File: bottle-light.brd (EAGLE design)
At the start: 160 x 100 mm, 49 parts, among them IC1 STM32F334K8T, IC2 LF33, T1 BC337, T2 BC337, T3 BC337

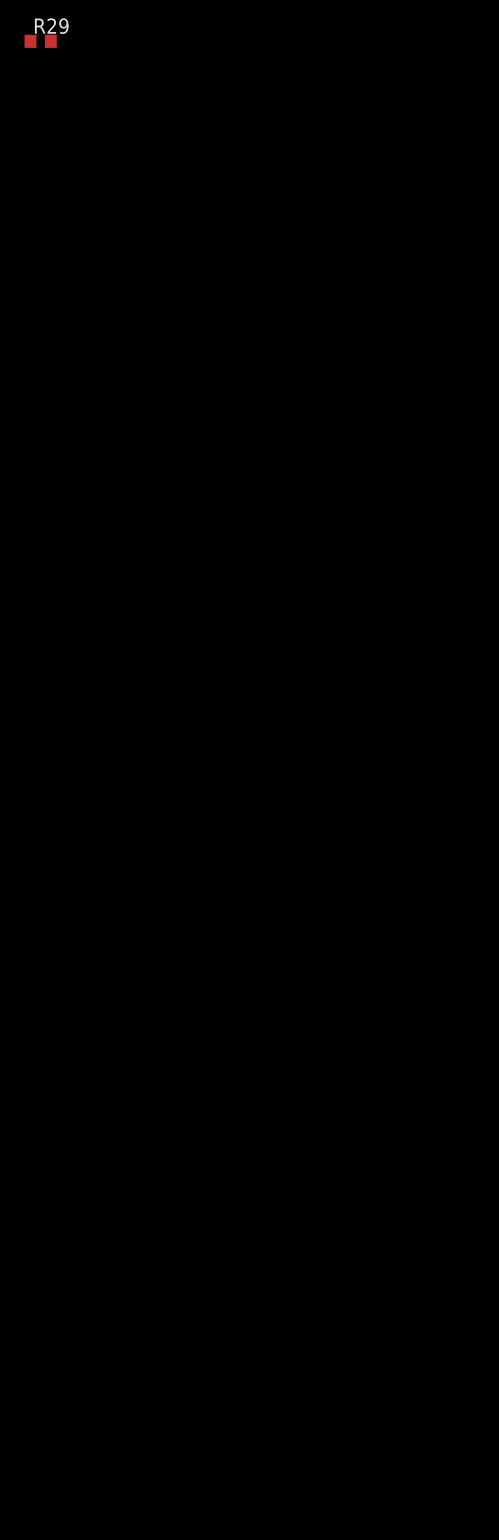
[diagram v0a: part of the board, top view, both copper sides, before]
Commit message: v0.1.1 worked on circuit diagram - new push buttons - new on/off button
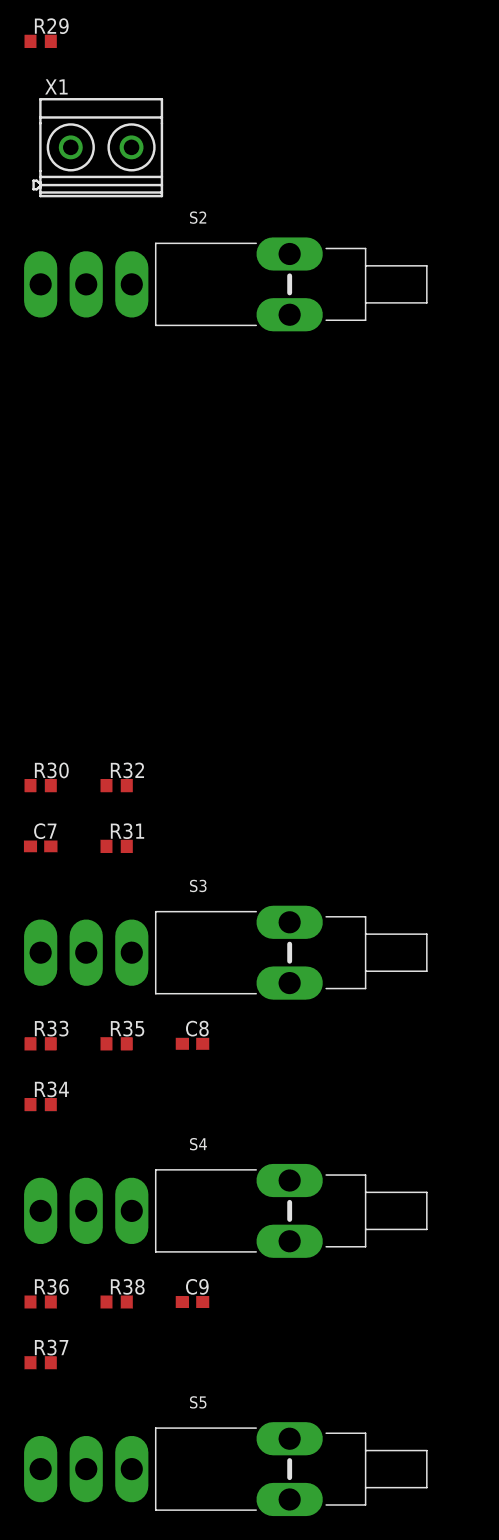
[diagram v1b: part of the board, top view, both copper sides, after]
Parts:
- added C7, C8, C9: 100n, resistor:C0603
- added R30, R33, R36: 100R, rcl:R0603
- added R31, R34, R37: 100k, rcl:R0603
- added R32, R35, R38: 330R, rcl:R0603
- added S2, S3, S4, S5: SPDT_PCB, h8-switch:SPDT_PCB
- added X1: 1725656, con-phoenix-508:MKDSN1,5/2-5,08
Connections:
- new net N$30: R30.1, R31.2, R32.2, S2.1
- new net N$31: C7.2, R30.2
- new net N$32: R33.1, R34.2, R35.2, S3.1
- new net N$33: C8.2, R33.2
- new net N$35: R36.1, R37.2, R38.2, S4.1
- new net N$36: C9.2, R36.2
- new net N$37: S5.1, X1.1
- new net USER-BUTTON1: R32.1
- new net USER-BUTTON2: R35.1
- new net USER-BUTTON3: R38.1
- net +3V3: now also C7.1, C8.1, C9.1, S2.2, S3.2, S4.2
- net +5V: now also S5.2
- net GND: now also R31.1, R34.1, R37.1, X1.2

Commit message: v0.1.2 Put in new devices and began routing pcb - new potis - made groundplane size for case - placed leds, potis and switch
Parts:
- LED1, LED2, LED3, LED4, LED5, LED6: value OSRAM_RGB-LED_LRTB-GFTM -> LRTB-GFTM
- R25, R26: value (none) -> RK09K; device pot:CIP20C-6MM -> h8-rlc:RK09K
- moved S2 158.4 mm to (7.00, 74.5), turned to 90 degrees
- moved R26 143.7 mm to (43.0, 83.5)
- moved LED3 108.9 mm to (58.0, 62.0)
- moved IC2 107.8 mm to (75.6, 59.3), turned to 180 degrees
- moved R25 105.2 mm to (25.0, 83.5)
- moved LED5 91.1 mm to (44.0, 46.0)
- moved LED4 90.2 mm to (66.0, 38.0)
- moved LED6 73.0 mm to (44.0, 22.0)
- moved LED1 68.9 mm to (22.0, 38.0)
- moved LED2 61.4 mm to (30.0, 62.0)
- moved IC1 0.38 mm to (-39.0, 5.00)
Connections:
- net +3V3: now also R25.3, R26.3; no longer R25.E, R26.E
- net GND: now also R25.1, R26.1; no longer R25.A, R26.A
- net POTI_COLOR: now also R25.2; no longer R25.S
- net POTI_LUMINOSITY: now also R26.2; no longer R26.S
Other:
- board size 160 x 100 mm -> 89 x 88 mm
- board text added: "Bottle Light | by HansAchterbahn v 0.1.2 | 09/07/2017"

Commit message: v0.1.3 schematic finished and board is routed - added new buttons - added swd debugger port - added battery pack - changed stm32 pinning - changed dc power supply port - removed reset button - added base resistors to transistors - routed board
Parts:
- removed S1: (no value), h8-switch:TACTILE-PTH
- removed X1: 1725656, con-phoenix-508:MKDSN1,5/2-5,08
- added JP1: SWD, h8-pinhead:2X03SMD
- added U$1: BARREL_CONNECTOR_3.5MM, h8-conector:BARREL_CONNECTOR_3.5MM
- added U1: KEYSTONE-2481, h8-misc:KEYSTONE-2481
- R23, R24: value 8.2 -> 560
- R27: value 8.2 -> 270
- S2, S3, S4: value SPDT_PCB -> ALPS-SKHH; device h8-switch:SPDT_PCB -> h8-switch:ALPS-SKHH
- moved R37 277.7 mm to (78.0, 74.0), flipped to the bottom, turned to 90 degrees
- moved R36 276.6 mm to (82.0, 74.0), flipped to the bottom, turned to 270 degrees
- moved R38 271.0 mm to (80.0, 74.0), flipped to the bottom, turned to 90 degrees
- moved S4 270.0 mm to (81.0, 80.5), turned to 180 degrees
- moved C9 269.4 mm to (84.0, 74.0), flipped to the bottom, turned to 270 degrees
- moved R34 253.6 mm to (66.0, 74.0), flipped to the bottom, turned to 90 degrees
- moved R33 252.7 mm to (70.0, 74.0), flipped to the bottom, turned to 270 degrees
- moved R35 246.9 mm to (68.0, 74.0), flipped to the bottom, turned to 90 degrees
- moved S3 245.9 mm to (69.0, 80.5), turned to 180 degrees
- moved C8 245.3 mm to (72.0, 74.0), flipped to the bottom, turned to 270 degrees
- moved S5 245.2 mm to (15.5, 74.5), turned to 90 degrees
- moved C7 234.0 mm to (60.0, 74.0), flipped to the bottom, turned to 270 degrees
- moved R30 229.0 mm to (58.0, 74.0), flipped to the bottom, turned to 270 degrees
- moved R31 225.3 mm to (54.0, 74.0), flipped to the bottom, turned to 90 degrees
- moved R32 223.0 mm to (56.0, 74.0), flipped to the bottom, turned to 90 degrees
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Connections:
- removed net N$37: S5.1, X1.1
- removed net SDW_IO: R20.1
- removed net SWD_CLK: R21.1
- removed net SWD_O: R22.1
- new net +6V: S5.1, U$1.1, U1.2
- new net SWD-CLK: JP1.2, R21.1
- new net SWD-IO: JP1.4, R20.1
- new net SWD-O: JP1.6, R22.1
- net +3V3: now also JP1.1
- net GND: now also JP1.3, U$1.2, U$1.3, U1.1; no longer S1.1, S1.2, X1.2
- net N$26: now also R23.2, T1.2; no longer IC1.6, R27.2
- net N$27: now also R24.2, T3.2; no longer IC1.8, R23.2
- net N$28: now also R27.2, T2.2; no longer IC1.9, R24.2
- net N$29: now also IC1.10, R29.2; no longer IC1.13, R28.2
- net N$34: now also IC1.11, R28.2; no longer IC1.14, R29.2
- net NRST: now also JP1.5; no longer S1.3, S1.4
- net PWM_B: now also IC1.30, R23.1; no longer R24.1, T1.2
- net PWM_G: now also IC1.28, R27.1; no longer R23.1, T2.2
- net PWM_R: now also IC1.27, R24.1; no longer R27.1, T3.2
- net USER-BUTTON1: now also IC1.18
- net USER-BUTTON2: now also IC1.19
- net USER-BUTTON3: now also IC1.20
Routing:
- net GND: track 0.00 -> 416.2 mm
- net +3V3: track 0.00 -> 254.8 mm, vias 0 -> 3
- net +5V: track 0.00 -> 186.6 mm
- net N$4: track 0.00 -> 149.1 mm, vias 0 -> 4
- net N$3: track 0.00 -> 146.5 mm, vias 0 -> 9
- net N$2: track 0.00 -> 131.7 mm, vias 0 -> 10
- net +6V: track 0.00 -> 88.8 mm
- net N$29: track 0.00 -> 63.7 mm
- net N$34: track 0.00 -> 46.8 mm
- net NRST: track 0.00 -> 44.3 mm, vias 0 -> 2
- net USER-BUTTON1: track 0.00 -> 42.6 mm, vias 0 -> 2
- net USER-BUTTON2: track 0.00 -> 34.7 mm, vias 0 -> 2
- net USER-BUTTON3: track 0.00 -> 27.1 mm, vias 0 -> 2
- net PWM_B: track 0.00 -> 24.8 mm
- net PWM_G: track 0.00 -> 24.7 mm
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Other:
- board size 89 x 88 mm -> 88 x 88 mm
- board text added: "Bottle Light | by HansAchterbahn v 0.1.3 | 10/07/2017"
- board text removed: "Bottle Light | by HansAchterbahn v 0.1.2 | 09/07/2017"

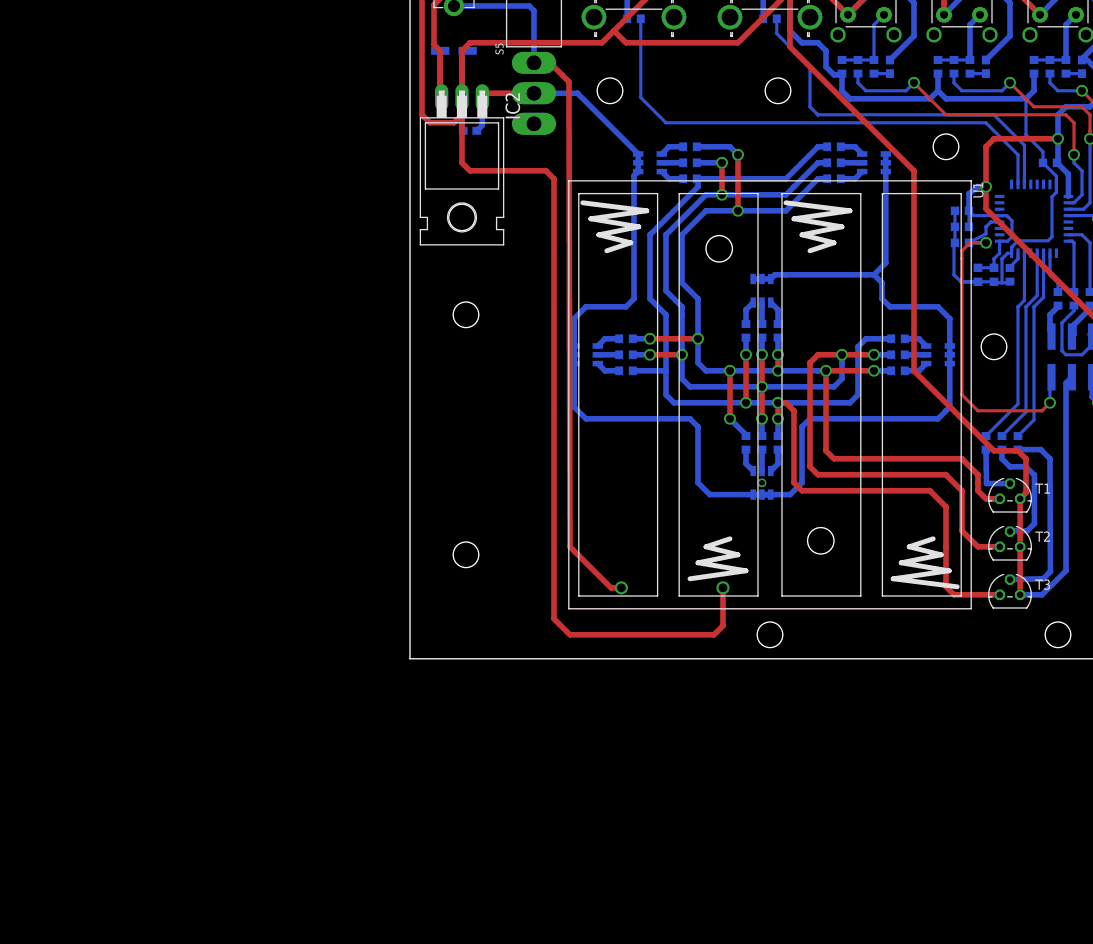
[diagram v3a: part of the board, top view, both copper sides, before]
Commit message: v0.2.0 Neue LEDs hinzugefügt: APA102
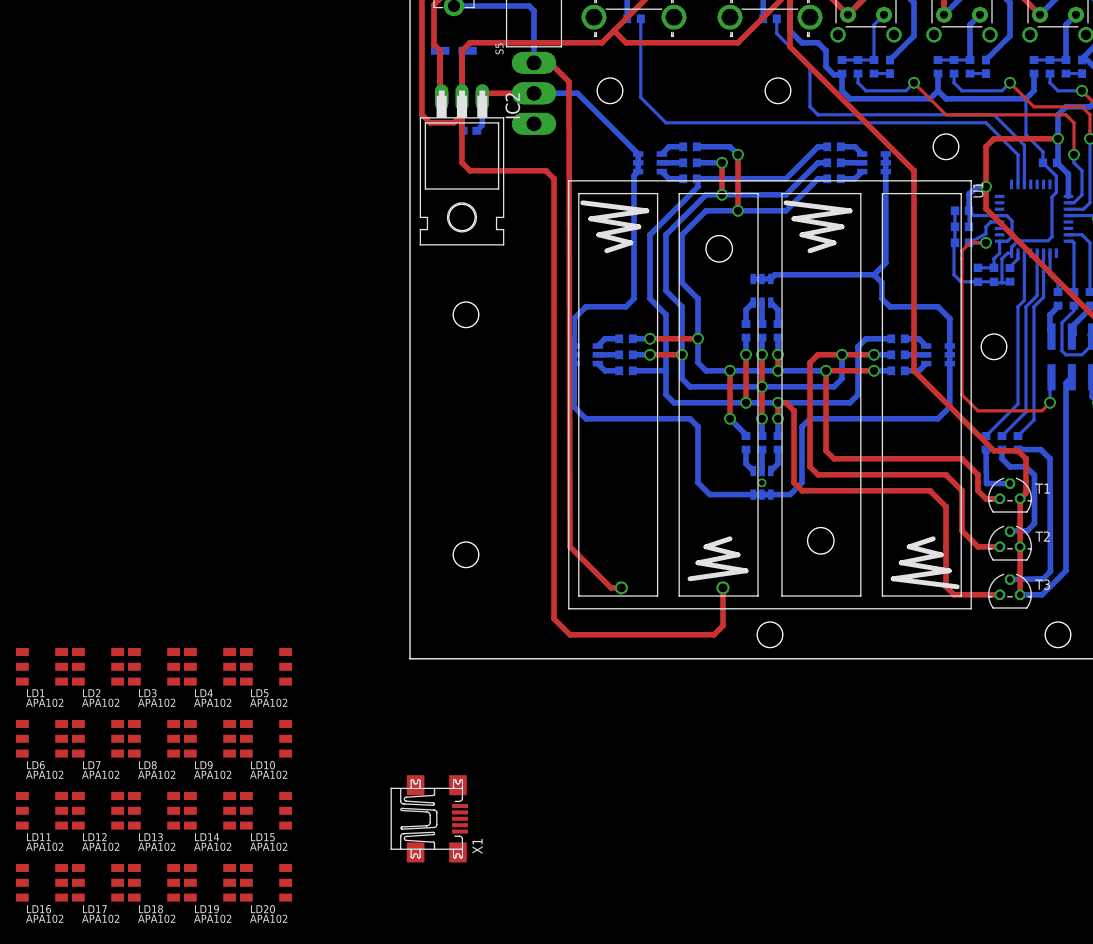
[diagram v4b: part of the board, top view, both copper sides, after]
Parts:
- added LD1, LD10, LD11, LD12, LD13, LD14, LD15, LD16, LD17, LD18, LD19, LD2, LD20, LD3, LD4, LD5, LD6, LD7, LD8, LD9: APA102, 3587:APA102C-5050
- added X1: MINI-USB-SHIELD-UX60A-MB-5ST, con-hirose:UX60A-MB-5ST
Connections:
- new net N$37: LD1.5, LD2.2
- new net N$39: LD1.4, LD2.1
- new net N$40: LD2.5, LD3.2
- new net N$41: LD2.4, LD3.1
- new net N$42: LD3.5, LD4.2
- new net N$43: LD3.4, LD4.1
- new net N$44: LD4.5, LD5.2
- new net N$45: LD4.4, LD5.1
- new net N$46: LD5.5, LD6.2
- new net N$47: LD5.4, LD6.1
- new net N$48: LD6.5, LD7.2
- new net N$49: LD6.4, LD7.1
- new net N$50: LD7.5, LD8.2
- new net N$51: LD7.4, LD8.1
- new net N$52: LD8.5, LD9.2
- new net N$53: LD8.4, LD9.1
- new net N$54: LD10.2, LD9.5
- new net N$55: LD10.1, LD9.4
- new net N$56: LD10.5, LD11.2
- new net N$57: LD10.4, LD11.1
- new net N$58: LD11.5, LD12.2
- new net N$59: LD11.4, LD12.1
- new net N$60: LD12.5, LD13.2
- new net N$61: LD12.4, LD13.1
- new net N$62: LD13.5, LD14.2
- new net N$63: LD13.4, LD14.1
- new net N$64: LD14.5, LD15.2
- new net N$65: LD14.4, LD15.1
- new net N$66: LD15.5, LD16.2
- new net N$67: LD15.4, LD16.1
- new net N$68: LD16.5, LD17.2
- new net N$69: LD16.4, LD17.1
- new net N$70: LD17.5, LD18.2
- new net N$71: LD17.4, LD18.1
- new net N$72: LD18.5, LD19.2
- new net N$73: LD18.4, LD19.1
- new net N$74: LD19.5, LD20.2
- new net N$75: LD19.4, LD20.1
- new net N$76: LD1.2
- new net N$77: LD1.1
- net +5V: now also LD1.6, LD10.6, LD11.6, LD12.6, LD13.6, LD14.6, LD15.6, LD16.6, LD17.6, LD18.6, LD19.6, LD2.6, LD20.6, LD3.6, LD4.6, LD5.6, LD6.6, LD7.6, LD8.6, LD9.6
- net GND: now also LD1.3, LD10.3, LD11.3, LD12.3, LD13.3, LD14.3, LD15.3, LD16.3, LD17.3, LD18.3, LD19.3, LD2.3, LD20.3, LD3.3, LD4.3, LD5.3, LD6.3, LD7.3, LD8.3, LD9.3
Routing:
- net GND: track 416.2 -> 411.7 mm

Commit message: v0.2.1 Die neuen LEDs positioniert
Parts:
- removed LD17, LD18, LD19, LD20: APA102, 3587:APA102C-5050
- removed LED1, LED2, LED3, LED4, LED5, LED6: LRTB-GFTM, h8-optic:OSRAM_RGB-LED_LRTB-GFTM
- removed R10, R11, R12, R13, R9: 91, resistor:R0603
- removed R14, R15, R16, R17, R18, R3: 300, resistor:R0603
- removed R23, R24: 560, resistor:R0603
- removed R27: 270, resistor:R0603
- removed R4, R5, R6, R7, R8: 200, resistor:R0603
- removed T1, T2, T3: BC337, transistor:TO92
- removed U1: KEYSTONE-2481, h8-misc:KEYSTONE-2481
- R1: value 200 -> 8.2
- R2: value 91 -> 8.2
- moved LD1 123.7 mm to (61.0, 61.0), flipped to the bottom
- moved LD6 113.2 mm to (50.0, 50.0), flipped to the bottom
- moved LD2 108.5 mm to (50.0, 61.0), flipped to the bottom
- moved LD13 104.2 mm to (61.0, 28.0), flipped to the bottom
- moved LD11 102.9 mm to (39.0, 39.0), flipped to the bottom
- moved X1 102.0 mm to (-10.0, 81.0), turned to 180 degrees
- moved LD9 99.0 mm to (61.0, 39.0), flipped to the bottom
- moved LD7 98.4 mm to (39.0, 50.0), flipped to the bottom
- moved LD3 94.3 mm to (39.0, 61.0), flipped to the bottom
- moved LD5 94.0 mm to (61.0, 50.0), flipped to the bottom
- moved LD16 92.8 mm to (28.0, 28.0), flipped to the bottom
- moved LD12 88.6 mm to (28.0, 39.0), flipped to the bottom
- moved LD14 88.5 mm to (50.0, 28.0), flipped to the bottom
- moved LD8 84.9 mm to (28.0, 50.0), flipped to the bottom
- moved LD10 83.8 mm to (50.0, 39.0), flipped to the bottom
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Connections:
- removed net +6V: S5.1, U$1.1, U1.2
- removed net N$10: LED2.C_R, R14.2
- removed net N$11: LED3.C_B, R5.2
- removed net N$12: LED3.C_G, R10.2
- removed net N$13: LED3.C_R, R15.2
- removed net N$14: LED4.C_B, R6.2
- removed net N$15: LED4.C_G, R11.2
- removed net N$16: LED4.C_R, R16.2
- removed net N$17: LED5.C_B, R7.2
- removed net N$18: LED5.C_G, R12.2
- removed net N$19: LED5.C_R, R17.2
- removed net N$20: LED6.C_B, R8.2
- removed net N$21: LED6.C_G, R13.2
- removed net N$22: LED6.C_R, R18.2
- removed net N$26: R23.2, T1.2
- removed net N$27: R24.2, T3.2
- removed net N$28: R27.2, T2.2
- removed net N$4: R14.1, R15.1, R16.1, R17.1, R18.1, R3.1, T3.3
- removed net N$5: LED1.C_B, R1.2
- removed net N$6: LED1.C_G, R2.2
- removed net N$68: LD16.5, LD17.2
- removed net N$69: LD16.4, LD17.1
- removed net N$7: LED1.C_R, R3.2
- removed net N$70: LD17.5, LD18.2
- removed net N$71: LD17.4, LD18.1
- removed net N$72: LD18.5, LD19.2
- removed net N$73: LD18.4, LD19.1
- removed net N$74: LD19.5, LD20.2
- removed net N$75: LD19.4, LD20.1
- removed net N$77: LD1.1
- removed net N$8: LED2.C_B, R4.2
- removed net N$9: LED2.C_G, R9.2
- removed net PWM_B: IC1.30, R23.1
- removed net PWM_G: IC1.28, R27.1
- removed net PWM_R: IC1.27, R24.1
- new net SPI-CLK: LD1.2, R1.1
- new net SPI-MOSI: LD1.1, R2.1
- net +5V: no longer LD17.6, LD18.6, LD19.6, LD20.6, LED1.A_B, LED1.A_G, LED1.A_R, LED2.A_B, LED2.A_G, LED2.A_R, LED3.A_B, LED3.A_G, LED3.A_R, LED4.A_B, LED4.A_G, LED4.A_R, LED5.A_B, LED5.A_G, LED5.A_R, LED6.A_B, LED6.A_G, LED6.A_R
- net GND: no longer LD17.3, LD18.3, LD19.3, LD20.3, T1.1, T2.1, T3.1, U$1.3, U1.1
- net N$2: now also IC1.11, R1.2; no longer R1.1, R4.1, R5.1, R6.1, R7.1, R8.1, T1.3
- net N$29: now also IC1.6; no longer IC1.10
- net N$3: now also IC1.13, R2.2; no longer R10.1, R11.1, R12.1, R13.1, R2.1, R9.1, T2.3
- net N$34: now also IC1.7; no longer IC1.11
- net N$76: now also S5.1, U$1.1; no longer LD1.2
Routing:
- net N$4: track 149.1 -> 0.00 mm, vias 4 -> 0
- net N$3: track 146.5 -> 0.00 mm, vias 9 -> 0
- net N$2: track 131.7 -> 0.00 mm, vias 10 -> 0
- net +6V: track 88.8 -> 0.00 mm
- net GND: track 411.7 -> 331.2 mm
- net PWM_B: track 24.8 -> 0.00 mm
- net PWM_G: track 24.7 -> 0.00 mm
- net PWM_R: track 24.2 -> 0.00 mm
- net N$27: track 24.0 -> 0.00 mm
- net +5V: track 186.6 -> 168.7 mm
- net N$76: track 0.00 -> 16.7 mm
- net N$28: track 15.6 -> 0.00 mm
- net N$26: track 7.19 -> 0.00 mm
- net N$67: track 0.00 -> 6.10 mm
- net N$66: track 0.00 -> 6.10 mm
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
